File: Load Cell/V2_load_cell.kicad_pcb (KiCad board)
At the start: 2 copper layers, 114.3 x 114.3 mm, 35 parts, among them J1 Conn_01x02, J10 Conn_01x06, J11 Conn_01x04, J12 Conn_01x06, J13 Conn_01x04, J14 Conn_01x06, J15 Conn_01x04, J16 Conn_01x06, J17 Conn_01x04, J2 Conn_01x06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

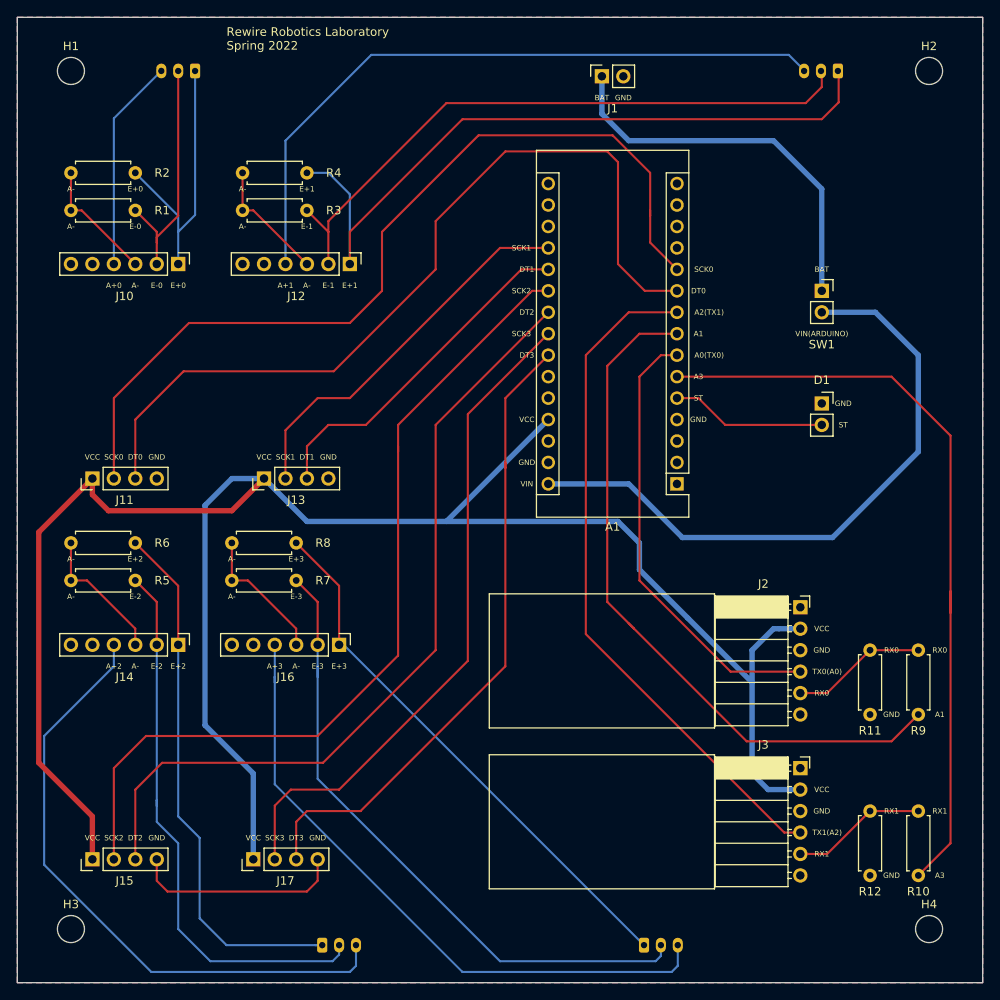
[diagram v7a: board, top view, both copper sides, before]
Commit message: changed some labels, redid traces, flipped JST, new zip
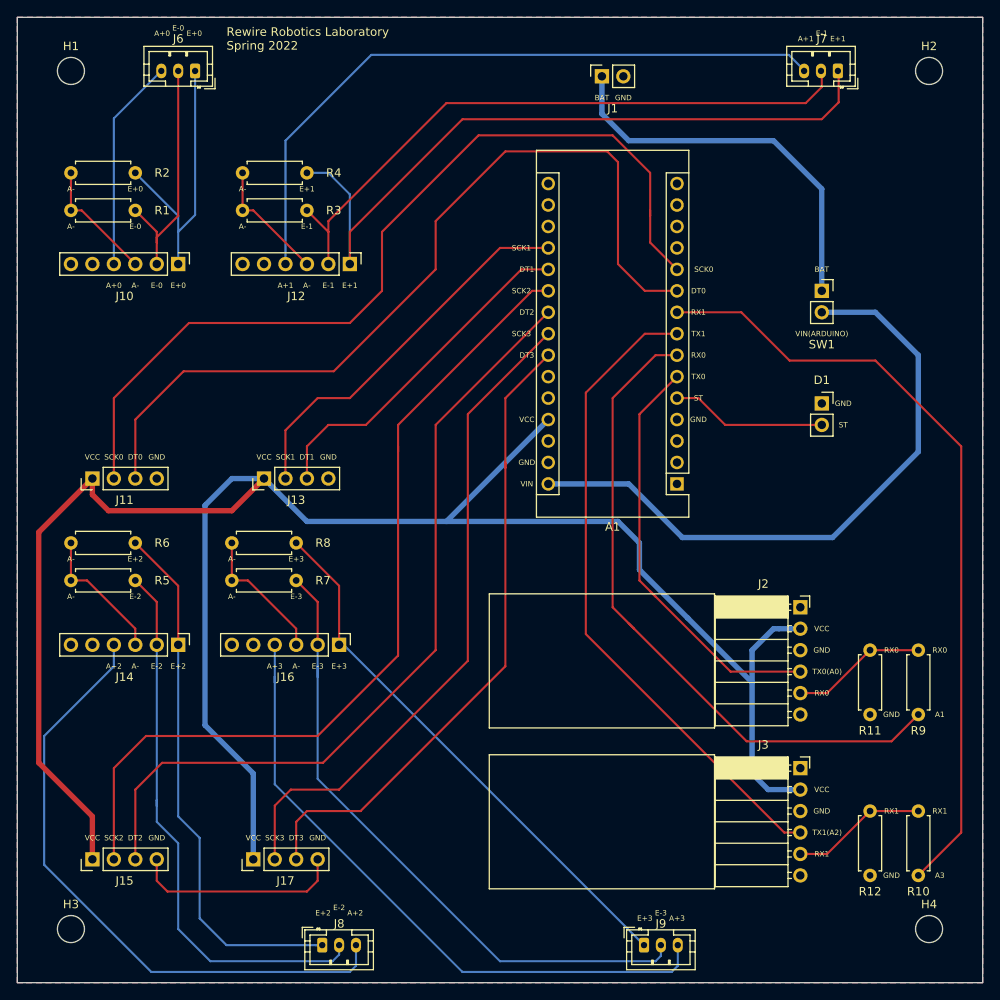
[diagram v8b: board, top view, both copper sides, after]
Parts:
- J6, J7, J8, J9: moved to F.Cu
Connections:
- A1 pad 6: /A3 -> /TX0
- A1 pad 7: /TX0 -> /RX0
- A1 pad 8: /A1 -> /TX1
- A1 pad 9: /TX1 -> /RX1
- J2 pad 5: /RX0 -> /RX0R
- J3 pad 5: /RX1 -> /RX1R
- R10 pad 1: /RX1 -> /RX1R
- R10 pad 2: /A3 -> /RX1
- R11 pad 1: /RX0 -> /RX0R
- R12 pad 2: /RX1 -> /RX1R
- R9 pad 1: /RX0 -> /RX0R
- R9 pad 2: /A1 -> /RX0
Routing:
- net /A3: track 91.5 -> 0.00 mm
- net /A1: track 83.7 -> 0.00 mm
- net /RX1: track 16.1 -> 93.1 mm
- net /RX0: track 16.1 -> 79.5 mm
- net /RX1R: track 0.00 -> 16.1 mm
- net /RX0R: track 0.00 -> 16.1 mm
- net /TX0: track 54.0 -> 50.4 mm
- net /TX1: track 81.1 -> 77.4 mm
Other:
- board text added: "TX0"
- board text added: "TX1"
- board text removed: "A0(TX0)"
- board text removed: "A2(TX1)"
